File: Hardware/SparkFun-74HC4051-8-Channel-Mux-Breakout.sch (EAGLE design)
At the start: 14 parts, among them U1 74HC4051BQ

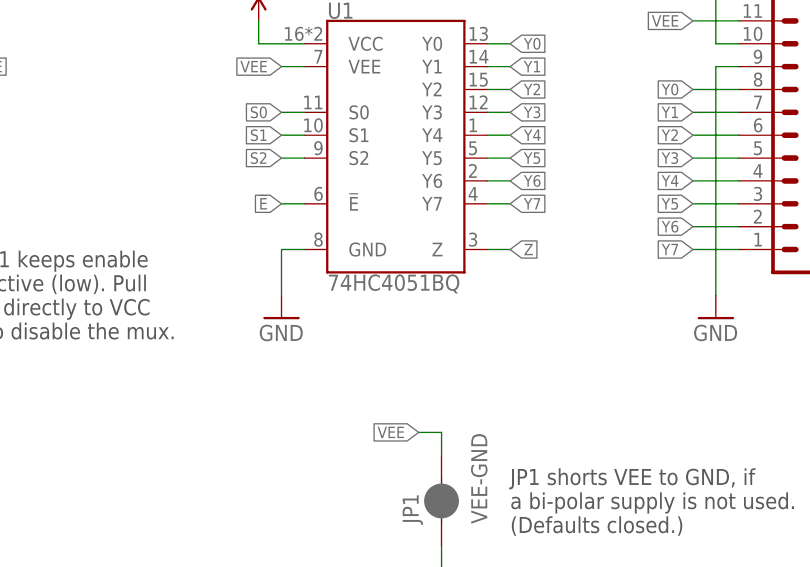
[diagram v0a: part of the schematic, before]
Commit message: Used improved SparkFun libraries to remove the need for separate library. Removed single part library. Resolves #3
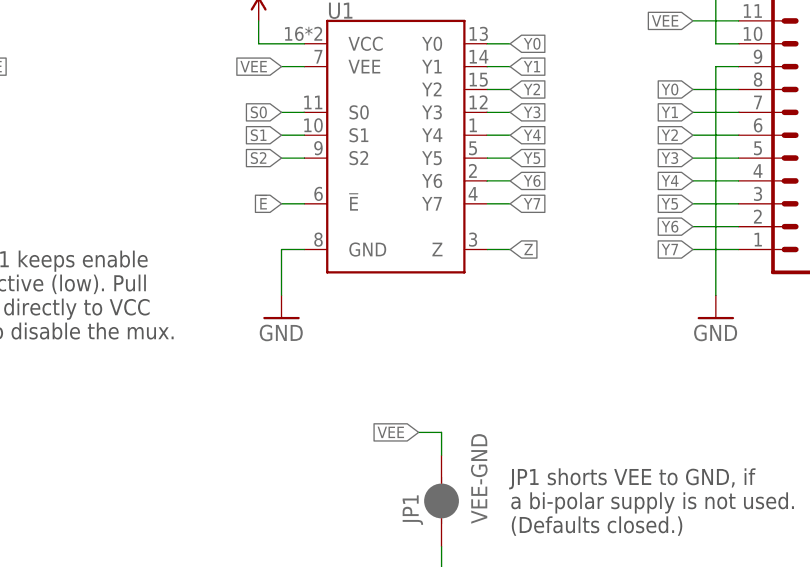
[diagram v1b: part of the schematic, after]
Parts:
- U1: value 74HC4051BQ -> (none); device 8mux:74HC4051BQ -> SparkFun-IC-Logic:74HC4051BQ
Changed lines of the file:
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@@
 <?xml version="1.0" encoding="utf-8"?>
 <!DOCTYPE eagle SYSTEM "eagle.dtd">
-<eagle version="7.5.0">
+<eagle version="7.7.0">
 <drawing>
 <settings>
@@
 <grid distance="0.1" unitdist="inch" unit="inch" style="lines" multiple="1" display="no" altdistance="0.01" altunitdist="inch" altunit="inch"/>
 <layers>
-<layer number="1" name="Top" color="4" fill="1" visible="no" active="no"/>
-<layer number="2" name="Route2" color="1" fill="3" visible="no" active="no"/>
-<layer number="3" name="Route3" color="4" fill="3" visible="no" active="no"/>
-<layer number="4" name="Route4" color="1" fill="4" visible="no" active="no"/>
-<layer number="5" name="Route5" color="4" fill="4" visible="no" active="no"/>
-<layer number="6" name="Route6" color="1" fill="8" visible="no" active="no"/>
-<layer number="7" name="Route7" color="4" fill="8" visible="no" active="no"/>
-<layer number="8" name="Route8" color="1" fill="2" visible="no" active="no"/>
-<layer number="9" name="Route9" color="4" fill="2" visible="no" active="no"/>
-<layer number="10" name="Route10" color="1" fill="7" visible="no" active="no"/>
-<layer number="11" name="Route11" color="4" fill="7" visible="no" active="no"/>
-<layer number="12" name="Route12" color="1" fill="5" visible="no" active="no"/>
-<layer number="13" name="Route13" color="4" fill="5" visible="no" active="no"/>
-<layer number="14" name="Route14" color="1" fill="6" visible="no" active="no"/>
-<layer number="15" name="Route15" color="4" fill="6" visible="no" active="no"/>
-<layer number="16" name="Bottom" color="1" fill="1" visible="no" active="no"/>
-<layer number="17" name="Pads" color="2" fill="1" visible="no" active="no"/>
-<layer number="18" name="Vias" color="2" fill="1" visible="no" active="no"/>
-<layer number="19" name="Unrouted" color="6" fill="1" visible="no" active="no"/>
-<layer number="20" name="Dimension" color="15" fill="1" visible="no" active="no"/>
-<layer number="21" name="tPlace" color="16" fill="1" visible="no" active="no"/>
-<layer number="22" name="bPlace" color="14" fill="1" visible="no" active="no"/>
-<layer number="23" name="tOrigins" color="15" fill="1" visible="no" active="no"/>
-<layer number="24" name="bOrigins" color="15" fill="1" visible="no" active="no"/>
-<layer number="25" name="tNames" color="7" fill="1" visible="no" active="no"/>
-<layer number="26" name="bNames" color="7" fill="1" visible="no" active="no"/>
-<layer number="27" name="tValues" color="7" fill="1" visible="no" active="no"/>
-<layer number="28" name="bValues" color="7" fill="1" visible="no" active="no"/>
+<layer number="1" name="Top" color="4" fill="1" visible="yes" active="no"/>
+<layer number="2" name="Route2" color="1" fill="3" visible="yes" active="no"/>
+<layer number="3" name="Route3" color="4" fill="3" visible="yes" active="no"/>
+<layer number="4" name="Route4" color="1" fill="4" visible="yes" active="no"/>
+<layer number="5" name="Route5" color="4" fill="4" visible="yes" active="no"/>
+<layer number="6" name="Route6" color="1" fill="8" visible="yes" active="no"/>
+<layer number="7" name="Route7" color="4" fill="8" visible="yes" active="no"/>
+<layer number="8" name="Route8" color="1" fill="2" visible="yes" active="no"/>
+<layer number="9" name="Route9" color="4" fill="2" visible="yes" active="no"/>
+<layer number="10" name="Route10" color="1" fill="7" visible="yes" active="no"/>
+<layer number="11" name="Route11" color="4" fill="7" visible="yes" active="no"/>
+<layer number="12" name="Route12" color="1" fill="5" visible="yes" active="no"/>
+<layer number="13" name="Route13" color="4" fill="5" visible="yes" active="no"/>
+<layer number="14" name="Route14" color="1" fill="6" visible="yes" active="no"/>
+<layer number="15" name="Route15" color="4" fill="6" visible="yes" active="no"/>
+<layer number="16" name="Bottom" color="1" fill="1" visible="yes" active="no"/>
+<layer number="17" name="Pads" color="2" fill="1" visible="yes" active="no"/>
+<layer number="18" name="Vias" color="2" fill="1" visible="yes" active="no"/>
+<layer number="19" name="Unrouted" color="6" fill="1" visible="yes" active="no"/>
+<layer number="20" name="Dimension" color="15" fill="1" visible="yes" active="no"/>
+<layer number="21" name="tPlace" color="16" fill="1" visible="yes" active="no"/>
+<layer number="22" name="bPlace" color="14" fill="1" visible="yes" active="no"/>
+<layer number="23" name="tOrigins" color="15" fill="1" visible="yes" active="no"/>
+<layer number="24" name="bOrigins" color="15" fill="1" visible="yes" active="no"/>
+<layer number="25" name="tNames" color="7" fill="1" visible="yes" active="no"/>
+<layer number="26" name="bNames" color="7" fill="1" visible="yes" active="no"/>
+<layer number="27" name="tValues" color="7" fill="1" visible="yes" active="no"/>
+<layer number="28" name="bValues" color="7" fill="1" visible="yes" active="no"/>
 <layer number="29" name="tStop" color="7" fill="3" visible="no" active="no"/>
 <layer number="30" name="bStop" color="7" fill="6" visible="no" active="no"/>
@@
 <layer number="35" name="tGlue" color="7" fill="4" visible="no" active="no"/>
 <layer number="36" name="bGlue" color="7" fill="5" visible="no" active="no"/>
-<layer number="37" name="tTest" color="7" fill="1" visible="no" active="no"/>
-<layer number="38" name="bTest" color="7" fill="1" visible="no" active="no"/>
+<layer number="37" name="tTest" color="7" fill="1" visible="yes" active="no"/>
+<layer number="38" name="bTest" color="7" fill="1" visible="yes" active="no"/>
 <layer number="39" name="tKeepout" color="4" fill="11" visible="no" active="no"/>
 <layer number="40" name="bKeepout" color="1" fill="11" visible="no" active="no"/>
@@
 <layer number="44" name="Drills" color="7" fill="1" visible="no" active="no"/>
 <layer number="45" name="Holes" color="7" fill="1" visible="no" active="no"/>
-<layer number="46" name="Milling" color="3" fill="1" visible="no" active="no"/>
-<layer number="47" name="Measures" color="7" fill="1" visible="no" active="no"/>
-<layer number="48" name="Document" color="7" fill="1" visible="no" active="no"/>
-<layer number="49" name="Reference" color="7" fill="1" visible="no" active="no"/>
-<layer number="50" name="dxf" color="7" fill="1" visible="no" active="no"/>
-<layer number="51" name="tDocu" color="6" fill="1" visible="no" active="no"/>
-<layer number="52" name="bDocu" color="7" fill="1" visible="no" active="no"/>
-<layer number="53" name="tGND_GNDA" color="7" fill="9" visible="no" active="no"/>
-<layer number="54" name="bGND_GNDA" color="1" fill="9" visible="no" active="no"/>
-<layer number="56" name="wert" color="7" fill="1" visible="no" active="no"/>
-<layer number="57" name="tCAD" color="7" fill="1" visible="no" active="no"/>
-<layer number="59" name="tCarbon" color="7" fill="1" visible="no" active="no"/>
-<layer number="60" name="bCarbon" color="7" fill="1" visible="no" active="no"/>
+<layer number="46" name="Milling" color="3" fill="1" visible="yes" active="no"/>
+<layer number="47" name="Measures" color="7" fill="1" visible="yes" active="no"/>
+<layer number="48" name="Document" color="7" fill="1" visible="yes" active="no"/>
+<layer number="49" name="Reference" color="7" fill="1" visible="yes" active="no"/>
+<layer number="50" name="dxf" color="7" fill="1" visible="yes" active="no"/>
+<layer number="51" name="tDocu" color="6" fill="1" visible="yes" active="no"/>
+<layer number="52" name="bDocu" color="7" fill="1" visible="yes" active="no"/>
+<layer number="53" name="tGND_GNDA" color="7" fill="9" visible="yes" active="no"/>
+<layer number="54" name="bGND_GNDA" color="1" fill="9" visible="yes" active="no"/>
+<layer number="56" name="wert" color="7" fill="1" visible="yes" active="no"/>
+<layer number="57" name="tCAD" color="7" fill="1" visible="yes" active="no"/>
+<layer number="59" name="tCarbon" color="7" fill="1" visible="yes" active="no"/>
+<layer number="60" name="bCarbon" color="7" fill="1" visible="yes" active="no"/>
 <layer number="90" name="Modules" color="5" fill="1" visible="yes" active="yes"/>
 <layer number="91" name="Nets" color="2" fill="1" visible="yes" active="yes"/>
@@
 </classes>
 <parts>
-<part name="U1" library="8mux" deviceset="74HC4051" device="BQ"/>
+<part name="U1" library="SparkFun-IC-Logic" deviceset="74*4051" device="BQ" technology="HC"/>
 <part name="FRAME1" library="SparkFun-Aesthetics" deviceset="FRAME-LETTER" device=""/>
 <part name="C1" library="SparkFun-Capacitors" deviceset="0.1UF" device="-0603-25V-(+80/-20%)" value="0.1uF"/>
